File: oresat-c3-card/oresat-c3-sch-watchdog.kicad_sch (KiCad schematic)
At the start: 35 parts, among them U28 TLV1704-SEP

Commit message: Updating BOM and switching to oresat-passive footprints. Fixed some power cutoff limits, and fixed another DC voltage leverl on an LNA!
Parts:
- D1, D3, D9: DST Digi-Key -> DigiKey
- R31: footprint Resistor_SMD:R_1206_3216Metric -> oresat-passives:1206-C; DPN RHM10.0AFCT-ND -> RMCF1206FT10R0CT-ND; DST Digi-Key -> DigiKey; MFR Rohm Semiconductor -> Stackpole Electronics Inc; MPN ESR18EZPF10R0 -> RMCF1206FT10R0
- R32, R34, R35, R38, R39, R41, R60, R61, R62, R64: footprint Resistor_SMD:R_0603_1608Metric -> oresat-passives:0603-C-NOSILK; DST Digi-Key -> DigiKey; MFR Stackpole Electronics Inc -> Stackpole Electronics
- R36, R37, R40, R58, R59, R63: footprint Resistor_SMD:R_0603_1608Metric -> oresat-passives:0603-C-NOSILK; DST Digi-Key -> DigiKey

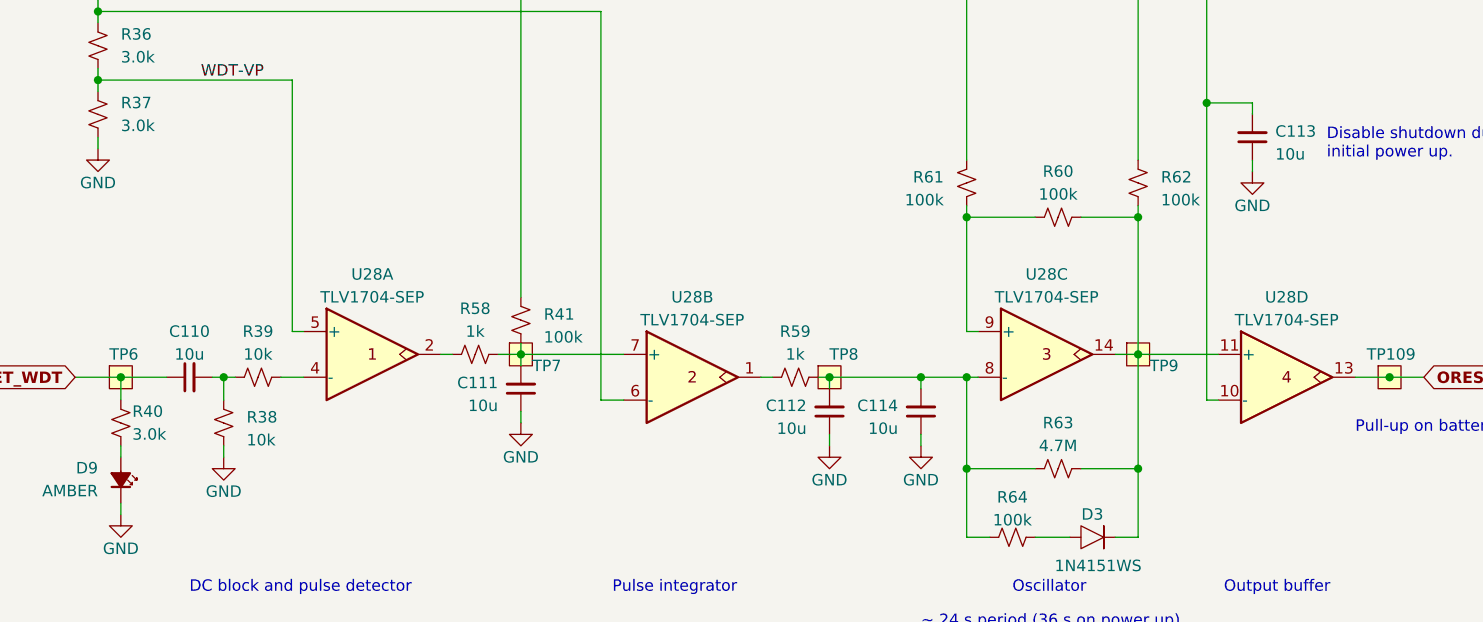
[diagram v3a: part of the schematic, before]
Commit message: All footprints updated. Passes ERC/DRC.
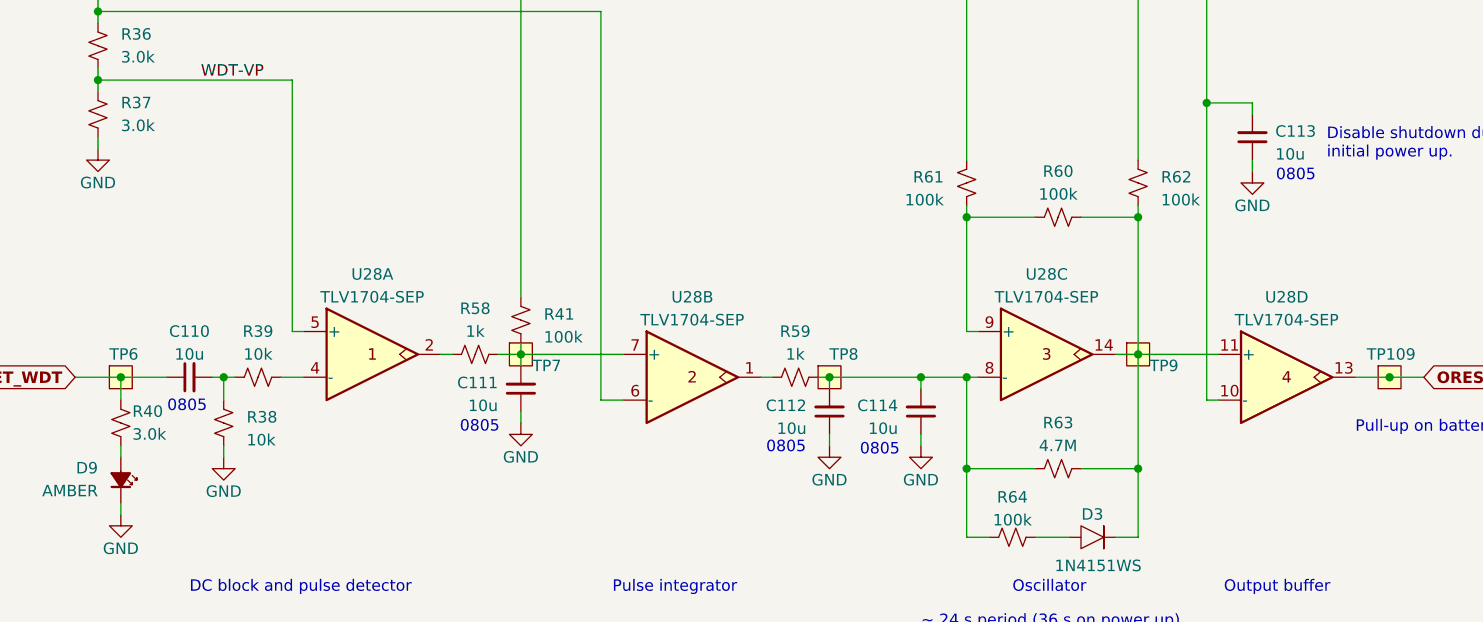
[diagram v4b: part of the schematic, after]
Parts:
- C110, C111, C112, C113, C114: footprint Capacitor_SMD:C_0603_1608Metric -> oresat-passives:0805-C-NOSILK; DPN 490-12317-1-ND -> 490-GRT21BC71E106KE13KCT-ND; DST Digi-Key -> DigiKey; MPN GRT188R61C106KE13D -> GRT21BC71E106KE13K
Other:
- note added: "0805"
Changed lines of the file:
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@@
 		(company "Portland State Aerospace Society")
 	)
+	(text "0805"
+		(exclude_from_sim no)
+		(at 308.356 142.748 0)
+		(effects
+			(font
+				(size 1.27 1.27)
+			)
+		)
+	)
 	(text "Pulse integrator"
 		(exclude_from_sim no)
@@
 		)
 	)
+	(text "0805"
+		(exclude_from_sim no)
+		(at 251.714 172.974 0)
+		(effects
+			(font
+				(size 1.27 1.27)
+			)
+		)
+	)
 	(text "DC block and pulse detector"
 		(exclude_from_sim no)
@@
 		)
 	)
+	(text "0805"
+		(exclude_from_sim no)
+		(at 262.128 173.228 0)
+		(effects
+			(font
+				(size 1.27 1.27)
+			)
+		)
+	)
+	(text "0805"
+		(exclude_from_sim no)
+		(at 185.166 168.402 0)
+		(effects
+			(font
+				(size 1.27 1.27)
+			)
+		)
+	)
+	(text "0805"
+		(exclude_from_sim no)
+		(at 217.678 170.688 0)
+		(effects
+			(font
+				(size 1.27 1.27)
+			)
+		)
+	)
 	(text "All resistors are 0603 1% AEC-Q200 unless marked.\nAll capacitors are 0603 AEC-Q200 Vw >= 16V X5R or better unless marked."
 		(exclude_from_sim no)
@@
 			)
 		)
-		(property "Footprint" "Capacitor_SMD:C_0603_1608Metric"
+		(property "Footprint" "oresat-passives:0805-C-NOSILK"
 			(at 303.53 138.43 0)
 			(effects
@@
 			)
 		)
-		(property "Datasheet" "~"
+		(property "Datasheet" "https://search.murata.co.jp/Ceramy/image/img/A01X/G101/ENG/GRT21BC71E106KE13-01.pdf"
 			(at 303.53 138.43 0)
 			(effects
@@
 			)
 		)
-		(property "Description" "10 µF ±10% 16V Ceramic Capacitor X5R 0603 (1608 Metric)"
+		(property "Description" "10 µF ±10% 25V Ceramic Capacitor X7S 0805 (2012 Metric)"
 			(at 303.53 138.43 0)
 			(effects
@@
 			)
 		)
-		(property "DPN" "490-12317-1-ND"
+		(property "DPN" "490-GRT21BC71E106KE13KCT-ND"
 			(at 303.53 138.43 0)
 			(effects
@@
 			)
 		)
-		(property "DST" "Digi-Key"
+		(property "DST" "DigiKey"
 			(at 303.53 138.43 0)
 			(effects
@@
 			)
 		)
-		(property "MPN" "GRT188R61C106KE13D"
+		(property "MPN" "GRT21BC71E106KE13K"
 			(at 303.53 138.43 0)
 			(effects
@@
 			)
 		)
-		(property "Footprint" "Capacitor_SMD:C_0603_1608Metric"
+		(property "Footprint" "oresat-passives:0805-C-NOSILK"
 			(at 222.25 166.37 0)
 			(effects
@@
 			)
 		)
-		(property "Datasheet" "~"
+		(property "Datasheet" "https://search.murata.co.jp/Ceramy/image/img/A01X/G101/ENG/GRT21BC71E106KE13-01.pdf"
 			(at 222.25 166.37 0)
 			(effects
@@
 			)
 		)
-		(property "Description" "10 µF ±10% 16V Ceramic Capacitor X5R 0603 (1608 Metric)"
+		(property "Description" "10 µF ±10% 25V Ceramic Capacitor X7S 0805 (2012 Metric)"
 			(at 222.25 166.37 0)
 			(effects
@@
 			)
 		)
-		(property "DPN" "490-12317-1-ND"
+		(property "DPN" "490-GRT21BC71E106KE13KCT-ND"
 			(at 222.25 166.37 0)
 			(effects
@@
 			)
 		)
-		(property "DST" "Digi-Key"
+		(property "DST" "DigiKey"
 			(at 222.25 166.37 0)
 			(effects
@@
 			)
 		)
-		(property "MPN" "GRT188R61C106KE13D"
+		(property "MPN" "GRT21BC71E106KE13K"
 			(at 222.25 166.37 0)
 			(effects
@@
 			)
 		)
-		(property "Footprint" "Capacitor_SMD:C_0603_1608Metric"
+		(property "Footprint" "oresat-passives:0805-C-NOSILK"
 			(at 266.7 168.91 0)
 			(effects
@@
 			)
 		)
-		(property "Datasheet" "~"
+		(property "Datasheet" "https://search.murata.co.jp/Ceramy/image/img/A01X/G101/ENG/GRT21BC71E106KE13-01.pdf"
 			(at 266.7 168.91 0)
 			(effects
@@
 			)
 		)
-		(property "Description" "10 µF ±10% 16V Ceramic Capacitor X5R 0603 (1608 Metric)"
+		(property "Description" "10 µF ±10% 25V Ceramic Capacitor X7S 0805 (2012 Metric)"
 			(at 266.7 168.91 0)
 			(effects
@@
 			)
 		)
-		(property "DPN" "490-12317-1-ND"
+		(property "DPN" "490-GRT21BC71E106KE13KCT-ND"
 			(at 266.7 168.91 0)
 			(effects
@@
 			)
 		)
-		(property "DST" "Digi-Key"
+		(property "DST" "DigiKey"
 			(at 266.7 168.91 0)
 			(effects
@@
 			)
 		)
-		(property "MPN" "GRT188R61C106KE13D"
+		(property "MPN" "GRT21BC71E106KE13K"
 			(at 266.7 168.91 0)
 			(effects
@@
 			)
 		)
-		(property "Footprint" "Capacitor_SMD:C_0603_1608Metric"
+		(property "Footprint" "oresat-passives:0805-C-NOSILK"
 			(at 256.54 168.91 0)
 			(effects
@@
 			)
 		)
-		(property "Datasheet" "~"
+		(property "Datasheet" "https://search.murata.co.jp/Ceramy/image/img/A01X/G101/ENG/GRT21BC71E106KE13-01.pdf"
 			(at 256.54 168.91 0)
 			(effects
@@
 			)
 		)
-		(property "Description" "10 µF ±10% 16V Ceramic Capacitor X5R 0603 (1608 Metric)"
+		(property "Description" "10 µF ±10% 25V Ceramic Capacitor X7S 0805 (2012 Metric)"
 			(at 256.54 168.91 0)
 			(effects
@@
 			)
 		)
-		(property "DPN" "490-12317-1-ND"
+		(property "DPN" "490-GRT21BC71E106KE13KCT-ND"
 			(at 256.54 168.91 0)
 			(effects
@@
 			)
 		)
-		(property "DST" "Digi-Key"
+		(property "DST" "DigiKey"
 			(at 256.54 168.91 0)
 			(effects
@@
 			)
 		)
-		(property "MPN" "GRT188R61C106KE13D"
+		(property "MPN" "GRT21BC71E106KE13K"
 			(at 256.54 168.91 0)
 			(effects
@@
 			)
 		)
-		(property "Footprint" "Capacitor_SMD:C_0603_1608Metric"
+		(property "Footprint" "oresat-passives:0805-C-NOSILK"
 			(at 185.42 165.1 0)
 			(effects
@@
 			)
 		)
-		(property "Datasheet" "~"
+		(property "Datasheet" "https://search.murata.co.jp/Ceramy/image/img/A01X/G101/ENG/GRT21BC71E106KE13-01.pdf"
 			(at 185.42 165.1 0)
 			(effects
@@
 			)
 		)
-		(property "Description" "10 µF ±10% 16V Ceramic Capacitor X5R 0603 (1608 Metric)"
+		(property "Description" "10 µF ±10% 25V Ceramic Capacitor X7S 0805 (2012 Metric)"
 			(at 185.42 165.1 0)
 			(effects
@@
 			)
 		)
-		(property "DPN" "490-12317-1-ND"
+		(property "DPN" "490-GRT21BC71E106KE13KCT-ND"
 			(at 185.42 165.1 0)
 			(effects
@@
 			)
 		)
-		(property "DST" "Digi-Key"
+		(property "DST" "DigiKey"
 			(at 185.42 165.1 0)
 			(effects
@@
 			)
 		)
-		(property "MPN" "GRT188R61C106KE13D"
+		(property "MPN" "GRT21BC71E106KE13K"
 			(at 185.42 165.1 0)
 			(effects
